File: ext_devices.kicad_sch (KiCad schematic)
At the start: 24 parts, among them CON1 MIKROBUS_HOST_CONN, J14 Conn_01x08_Female, J15 Conn_01x08_Female, U12 TXS0102DCU, U13 TXS0102DCU, U16 SN74LV1T34DBV, U17 SN74LV1T34DBV, U18 SN74LV1T34DBV, U19 SN74LV1T34DBV, U20 SN74LV1T34DBV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

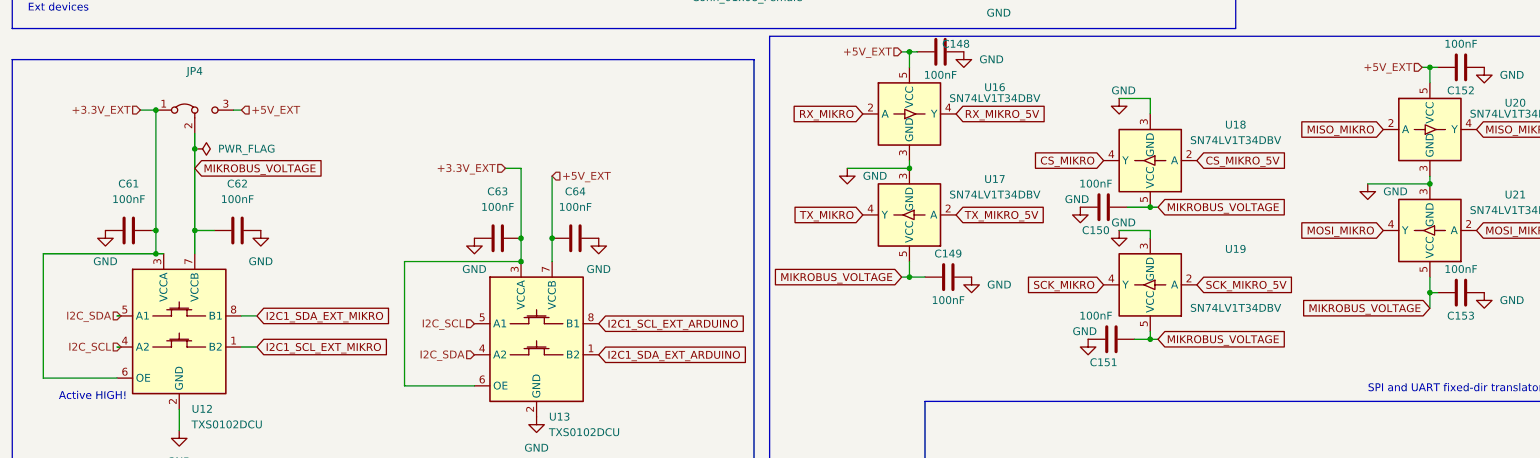
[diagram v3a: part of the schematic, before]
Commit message: Revert "fixed level shifter power"
This reverts commit a2797da565d1c7988ee84d7682cddb296432f328.
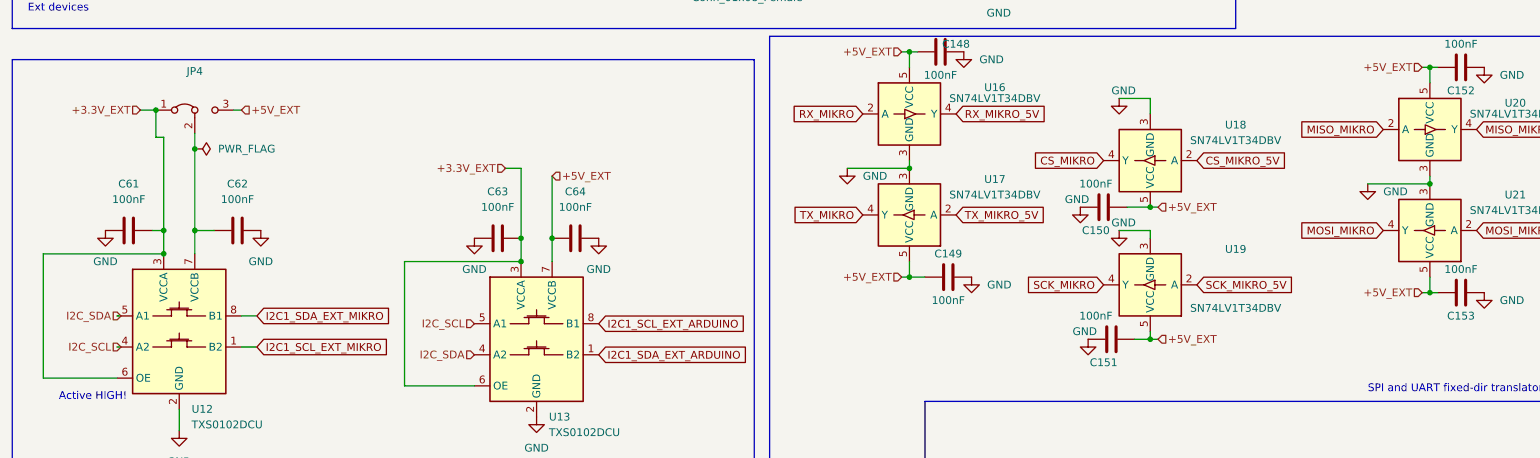
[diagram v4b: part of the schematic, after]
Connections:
- net +5V_EXT: now also C149.1, C150.2, C151.2, C153.1, U17.5 (VCC), U18.5 (VCC), U19.5 (VCC), U21.5 (VCC)
- removed net MIKROBUS_VOLTAGE: C149.1, C150.2, C151.2, C153.1, C62.1, JP4.2 (C), U12.7 (VCCB), U17.5 (VCC), U18.5 (VCC), U19.5 (VCC), U21.5 (VCC)
- new net: C62.1, JP4.2 (C), U12.7 (VCCB)
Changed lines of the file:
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@@
   (junction (at 114.3 137.16) (diameter 0) (color 0 0 0 0)
   )
-  (junction (at 49.53 139.7) (diameter 0) (color 0 0 0 0)
-  )
   (junction (at 109.22 137.16) (diameter 0) (color 0 0 0 0)
   )
+  (junction (at 50.8 135.89) (diameter 0) (color 0 0 0 0)
+  )
   (junction (at 49.53 116.205) (diameter 0) (color 0 0 0 0)
   )
@@
   (junction (at 109.22 140.97) (diameter 0) (color 0 0 0 0)
   )
+  (junction (at 50.8 139.7) (diameter 0) (color 0 0 0 0)
+  )
   (junction (at 187.325 93.98) (diameter 0) (color 0 0 0 0)
   )
@@
   )
   (junction (at 257.81 128.27) (diameter 0) (color 0 0 0 0)
-  )
-  (junction (at 49.53 135.89) (diameter 0) (color 0 0 0 0)
   )
   (junction (at 55.88 122.555) (diameter 0) (color 0 0 0 0)
@@
     (stroke (width 0) (type default) (color 0 0 0 0))
   )
-  (wire (pts (xy 49.53 135.89) (xy 49.53 139.7))
+  (wire (pts (xy 50.8 120.65) (xy 49.53 120.65))
+    (stroke (width 0) (type default) (color 0 0 0 0))
+  )
+  (wire (pts (xy 50.8 135.89) (xy 50.8 139.7))
     (stroke (width 0) (type default) (color 0 0 0 0))
   )
@@
     (stroke (width 0) (type default) (color 0 0 0 0))
   )
-  (wire (pts (xy 49.53 116.205) (xy 49.53 135.89))
+  (wire (pts (xy 49.53 116.205) (xy 49.53 120.65))
     (stroke (width 0) (type default) (color 0 0 0 0))
   )
@@
     (stroke (width 0) (type default) (color 0 0 0 0))
   )
-  (wire (pts (xy 257.81 148.59) (xy 257.81 146.05))
+  (wire (pts (xy 256.54 146.05) (xy 257.81 146.05))
     (stroke (width 0) (type default) (color 0 0 0 0))
   )
@@
     (stroke (width 0) (type default) (color 0 0 0 0))
   )
-  (wire (pts (xy 48.895 135.89) (xy 49.53 135.89))
+  (wire (pts (xy 48.895 135.89) (xy 50.8 135.89))
     (stroke (width 0) (type default) (color 0 0 0 0))
   )
@@
     (stroke (width 0) (type default) (color 0 0 0 0))
   )
-  (wire (pts (xy 49.53 139.7) (xy 50.8 139.7))
-    (stroke (width 0) (type default) (color 0 0 0 0))
-  )
   (wire (pts (xy 162.56 125.73) (xy 172.72 125.73))
     (stroke (width 0) (type default) (color 0 0 0 0))
@@
     (stroke (width 0) (type default) (color 0 0 0 0))
   )
+  (wire (pts (xy 50.8 120.65) (xy 50.8 135.89))
+    (stroke (width 0) (type default) (color 0 0 0 0))
+  )
   (wire (pts (xy 172.72 143.51) (xy 175.26 143.51))
     (stroke (width 0) (type default) (color 0 0 0 0))
@@
     (stroke (width 0) (type default) (color 0 0 0 0))
   )
-  (wire (pts (xy 31.115 139.7) (xy 49.53 139.7))
+  (wire (pts (xy 31.115 139.7) (xy 50.8 139.7))
     (stroke (width 0) (type default) (color 0 0 0 0))
   )
@@
     )
   )
-  (global_label "MIKROBUS_VOLTAGE" (shape input) (at 213.36 132.08 0) (fields_autoplaced)
-    (effects (font (size 1.27 1.27)) (justify left))
-    (property "Intersheet References" "${INTERSHEET_REFS}" (id 0) (at 234.3998 132.0006 0)
-      (effects (font (size 1.27 1.27)) (justify left) hide)
-    )
-  )
   (global_label "ARDUINO_A6" (shape input) (at 200.025 82.55 0) (fields_autoplaced)
     (effects (font (size 1.27 1.27)) (justify left))
@@
     )
   )
-  (global_label "MIKROBUS_VOLTAGE" (shape input) (at 213.36 153.67 0) (fields_autoplaced)
-    (effects (font (size 1.27 1.27)) (justify left))
-    (property "Intersheet References" "${INTERSHEET_REFS}" (id 0) (at 234.3998 153.5906 0)
-      (effects (font (size 1.27 1.27)) (justify left) hide)
-    )
-  )
   (global_label "TX_MIKRO_5V" (shape input) (at 174.625 54.61 180) (fields_autoplaced)
     (effects (font (size 1.27 1.27)) (justify right))
@@
     )
   )
-  (global_label "MIKROBUS_VOLTAGE" (shape input) (at 55.88 125.73 0) (fields_autoplaced)
-    (effects (font (size 1.27 1.27)) (justify left))
-    (property "Intersheet References" "${INTERSHEET_REFS}" (id 0) (at 76.9198 125.6506 0)
-      (effects (font (size 1.27 1.27)) (justify left) hide)
-    )
-  )
   (global_label "ARDUINO_D6" (shape input) (at 174.625 67.31 180) (fields_autoplaced)
     (effects (font (size 1.27 1.27)) (justify right))
@@
     )
   )
-  (global_label "MIKROBUS_VOLTAGE" (shape input) (at 257.81 148.59 180) (fields_autoplaced)
-    (effects (font (size 1.27 1.27)) (justify right))
-    (property "Intersheet References" "${INTERSHEET_REFS}" (id 0) (at 236.7702 148.6694 0)
-      (effects (font (size 1.27 1.27)) (justify right) hide)
-    )
-  )
   (global_label "AN_MIKRO" (shape input) (at 57.785 52.07 180) (fields_autoplaced)
     (effects (font (size 1.27 1.27)) (justify right))
@@
     )
   )
-  (global_label "MIKROBUS_VOLTAGE" (shape input) (at 171.45 143.51 180) (fields_autoplaced)
-    (effects (font (size 1.27 1.27)) (justify right))
-    (property "Intersheet References" "${INTERSHEET_REFS}" (id 0) (at 150.4102 143.5894 0)
-      (effects (font (size 1.27 1.27)) (justify right) hide)
-    )
-  )
   (global_label "MISO_MIKRO_5V" (shape input) (at 174.625 82.55 180) (fields_autoplaced)
     (effects (font (size 1.27 1.27)) (justify right))
@@
     (effects (font (size 1.27 1.27)) (justify right))
   )
+  (hierarchical_label "+5V_EXT" (shape input) (at 171.45 143.51 180)
+    (effects (font (size 1.27 1.27)) (justify right))
+  )
+  (hierarchical_label "+5V_EXT" (shape input) (at 213.36 132.08 0)
+    (effects (font (size 1.27 1.27)) (justify left))
+  )
   (hierarchical_label "I2C_SCL" (shape input) (at 101.6 151.13 180)
     (effects (font (size 1.27 1.27)) (justify right))
@@
     (effects (font (size 1.27 1.27)) (justify right))
   )
+  (hierarchical_label "+5V_EXT" (shape input) (at 256.54 146.05 180)
+    (effects (font (size 1.27 1.27)) (justify right))
+  )
   (hierarchical_label "I2C_SCL" (shape input) (at 43.815 154.94 180)
     (effects (font (size 1.27 1.27)) (justify right))
@@
     (effects (font (size 1.27 1.27)) (justify left))
   )
+  (hierarchical_label "+5V_EXT" (shape input) (at 213.36 153.67 0)
+    (effects (font (size 1.27 1.27)) (justify left))
+  )

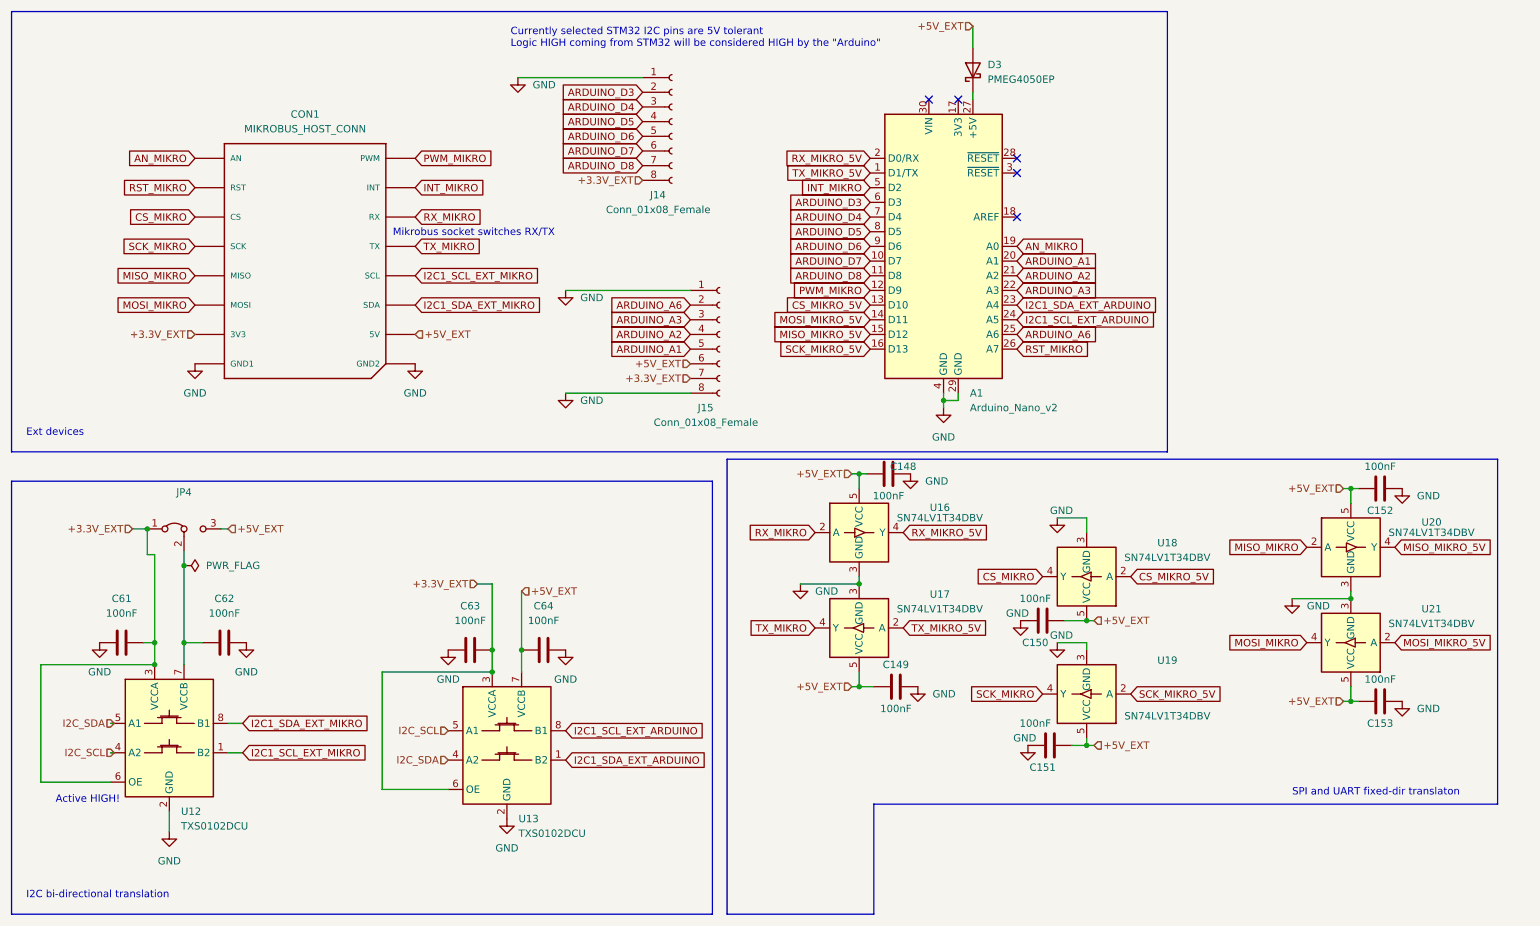
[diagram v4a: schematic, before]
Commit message: Revert "added level translation for UART and SPI"
This reverts commit 9eefb3982ed4f73a837f3bb03bd4a8073851e8e8.
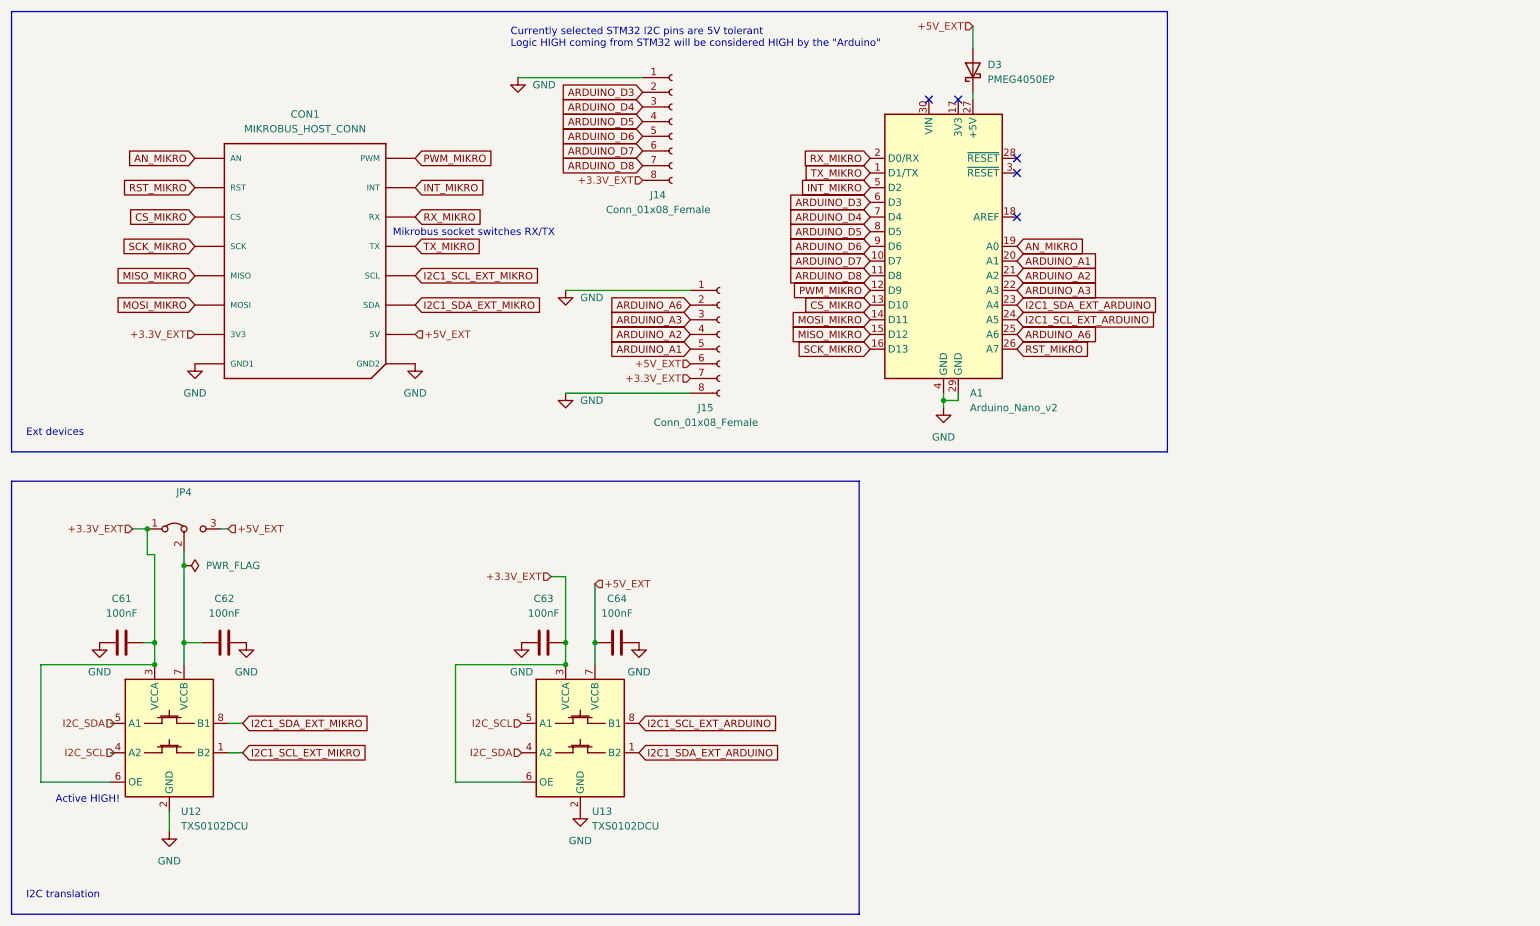
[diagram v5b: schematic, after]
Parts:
- removed C148, C149, C150, C151, C152, C153: 100nF, Capacitor_SMD:C_0402_1005Metric, symbol Device:C
- removed U16, U17, U18, U19, U20, U21: SN74LV1T34DBV, Package_TO_SOT_SMD:SOT-23-5, symbol Logic_LevelTranslator:SN74LV1T34DBV
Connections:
- net CS_MIKRO_5V is gone; now on net CS_MIKRO: A1.13 (D10)
- net MISO_MIKRO_5V is gone; now on net MISO_MIKRO: A1.15 (D12)
- net MOSI_MIKRO_5V is gone; now on net MOSI_MIKRO: A1.14 (D11)
- net RX_MIKRO_5V is gone; now on net RX_MIKRO: A1.2 (D0/RX)
- net SCK_MIKRO_5V is gone; now on net SCK_MIKRO: A1.16 (D13)
- net TX_MIKRO_5V is gone; now on net TX_MIKRO: A1.1 (D1/TX)
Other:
- note added: "I2C translation"
- note removed: "I2C bi-directional translation"
- note removed: "SPI and UART fixed-dir translaton"
- moved on the sheet: C63, C64, U13

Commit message: added level translation, missing silkscreen
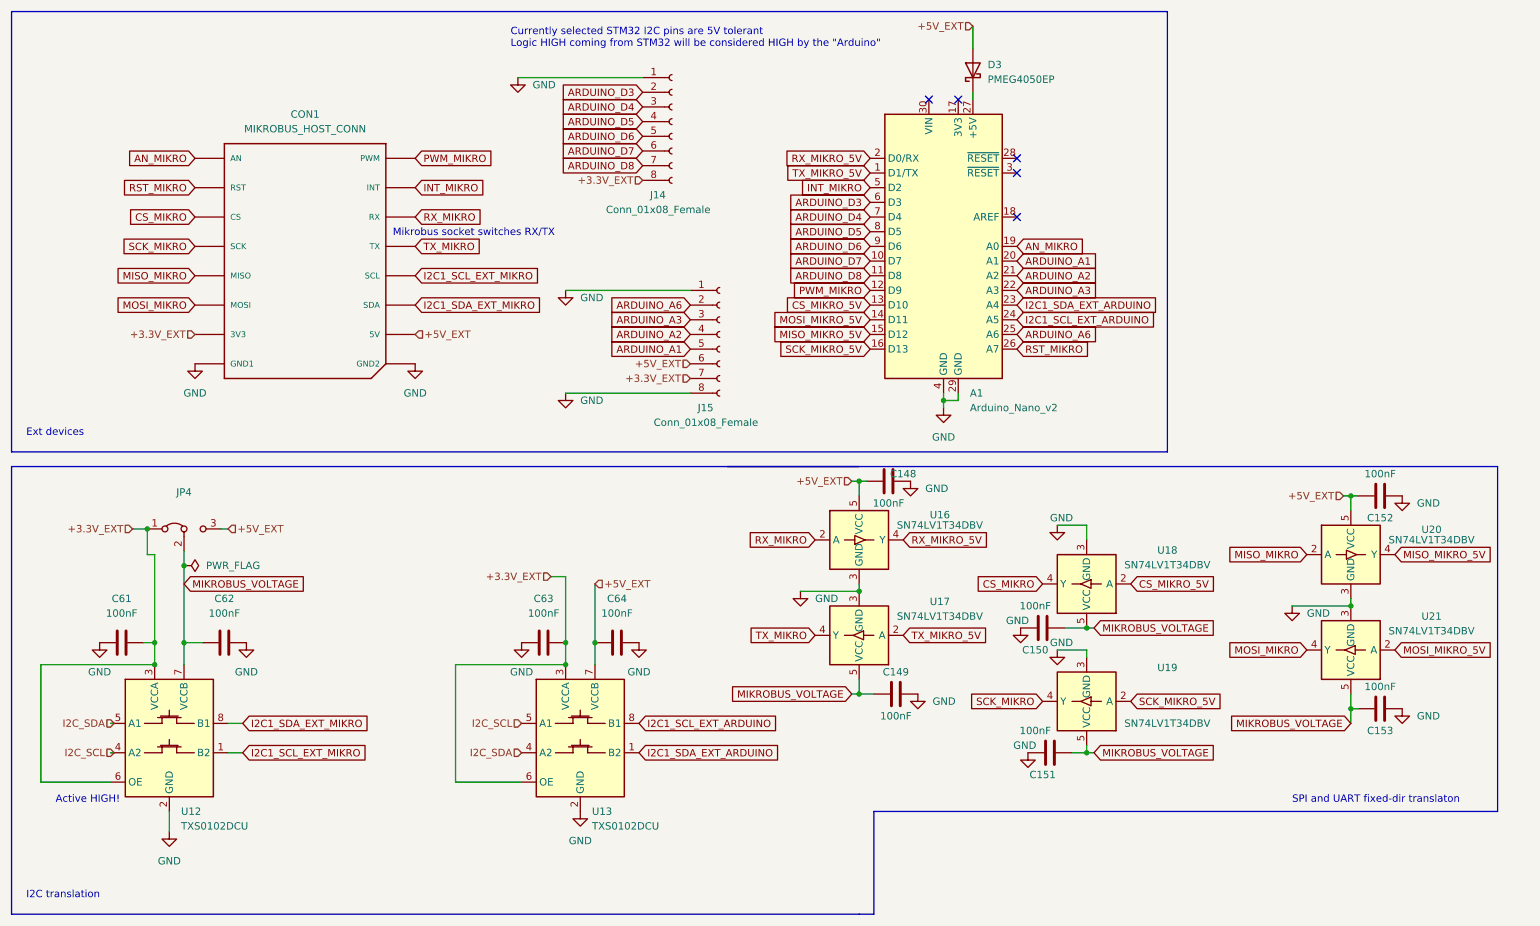
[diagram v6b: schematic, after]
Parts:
- added C148, C149, C150, C151, C152, C153: 100nF, Capacitor_SMD:C_0402_1005Metric, symbol Device:C
- added U16, U17, U18, U19, U20, U21: SN74LV1T34DBV, Package_TO_SOT_SMD:SOT-23-5, symbol Logic_LevelTranslator:SN74LV1T34DBV
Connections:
- net +5V_EXT: now also C148.1, C152.1, U16.5 (VCC), U20.5 (VCC)
- net CS_MIKRO: now also U18.4 (Y); no longer A1.13 (D10)
- net GND: now also C148.2, C149.2, C150.1, C151.1, C152.2, C153.2, U16.3 (GND), U17.3 (GND), U18.3 (GND), U19.3 (GND), U20.3 (GND), U21.3 (GND)
- net MISO_MIKRO: now also U20.2 (A); no longer A1.15 (D12)
- net MOSI_MIKRO: now also U21.4 (Y); no longer A1.14 (D11)
- net RX_MIKRO: now also U16.2 (A); no longer A1.2 (D0/RX)
- net SCK_MIKRO: now also U19.4 (Y); no longer A1.16 (D13)
- net TX_MIKRO: now also U17.4 (Y); no longer A1.1 (D1/TX)
- net MIKROBUS_VOLTAGE: now reaches C62.1, JP4.2 (C), U12.7 (VCCB)
- net MIKROBUS_VOLTAGE: now also C149.1, C150.2, C151.2, C153.1, U17.5 (VCC), U18.5 (VCC), U19.5 (VCC), U21.5 (VCC)
- new net CS_MIKRO_5V: A1.13 (D10), U18.2 (A)
- new net MISO_MIKRO_5V: A1.15 (D12), U20.4 (Y)
- new net MOSI_MIKRO_5V: A1.14 (D11), U21.2 (A)
- new net RX_MIKRO_5V: A1.2 (D0/RX), U16.4 (Y)
- new net SCK_MIKRO_5V: A1.16 (D13), U19.2 (A)
- new net TX_MIKRO_5V: A1.1 (D1/TX), U17.2 (A)
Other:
- note added: "SPI and UART fixed-dir translaton"
